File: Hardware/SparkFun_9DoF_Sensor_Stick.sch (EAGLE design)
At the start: 30 parts, among them U1 ITG-3200, U2 ADXL345, U4 3.3V

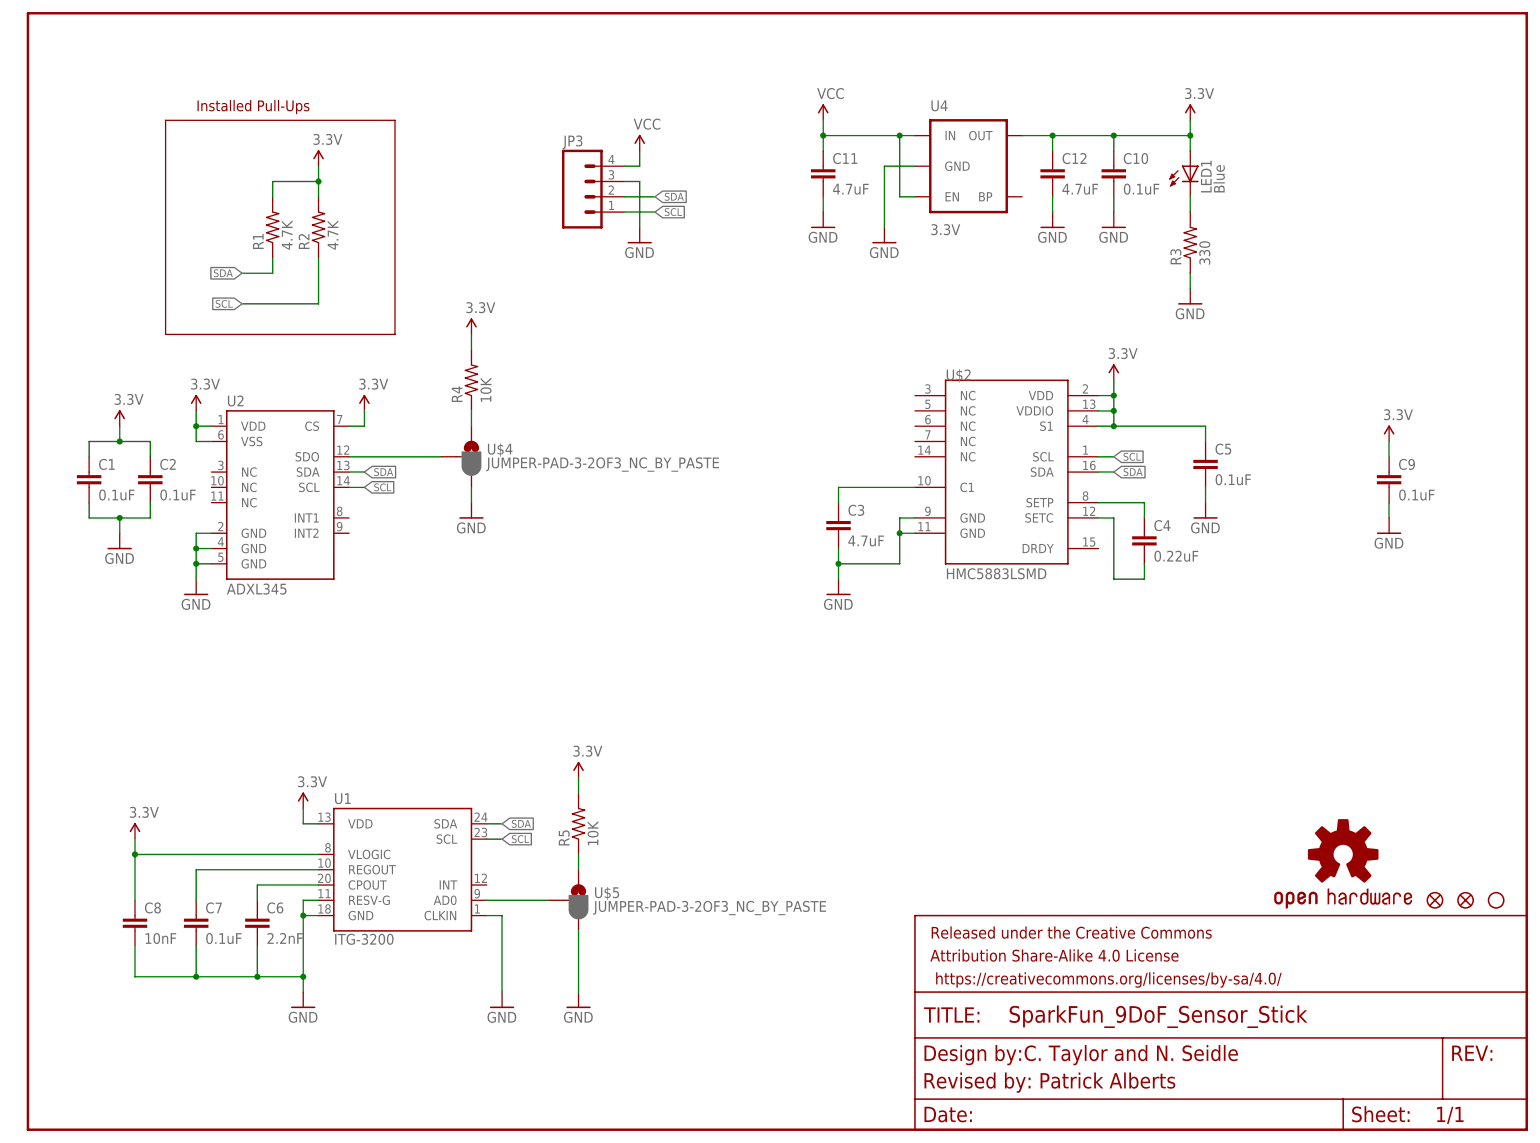
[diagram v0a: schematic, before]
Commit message: Adding in git files, updating to current boards on SF, cleaning up README
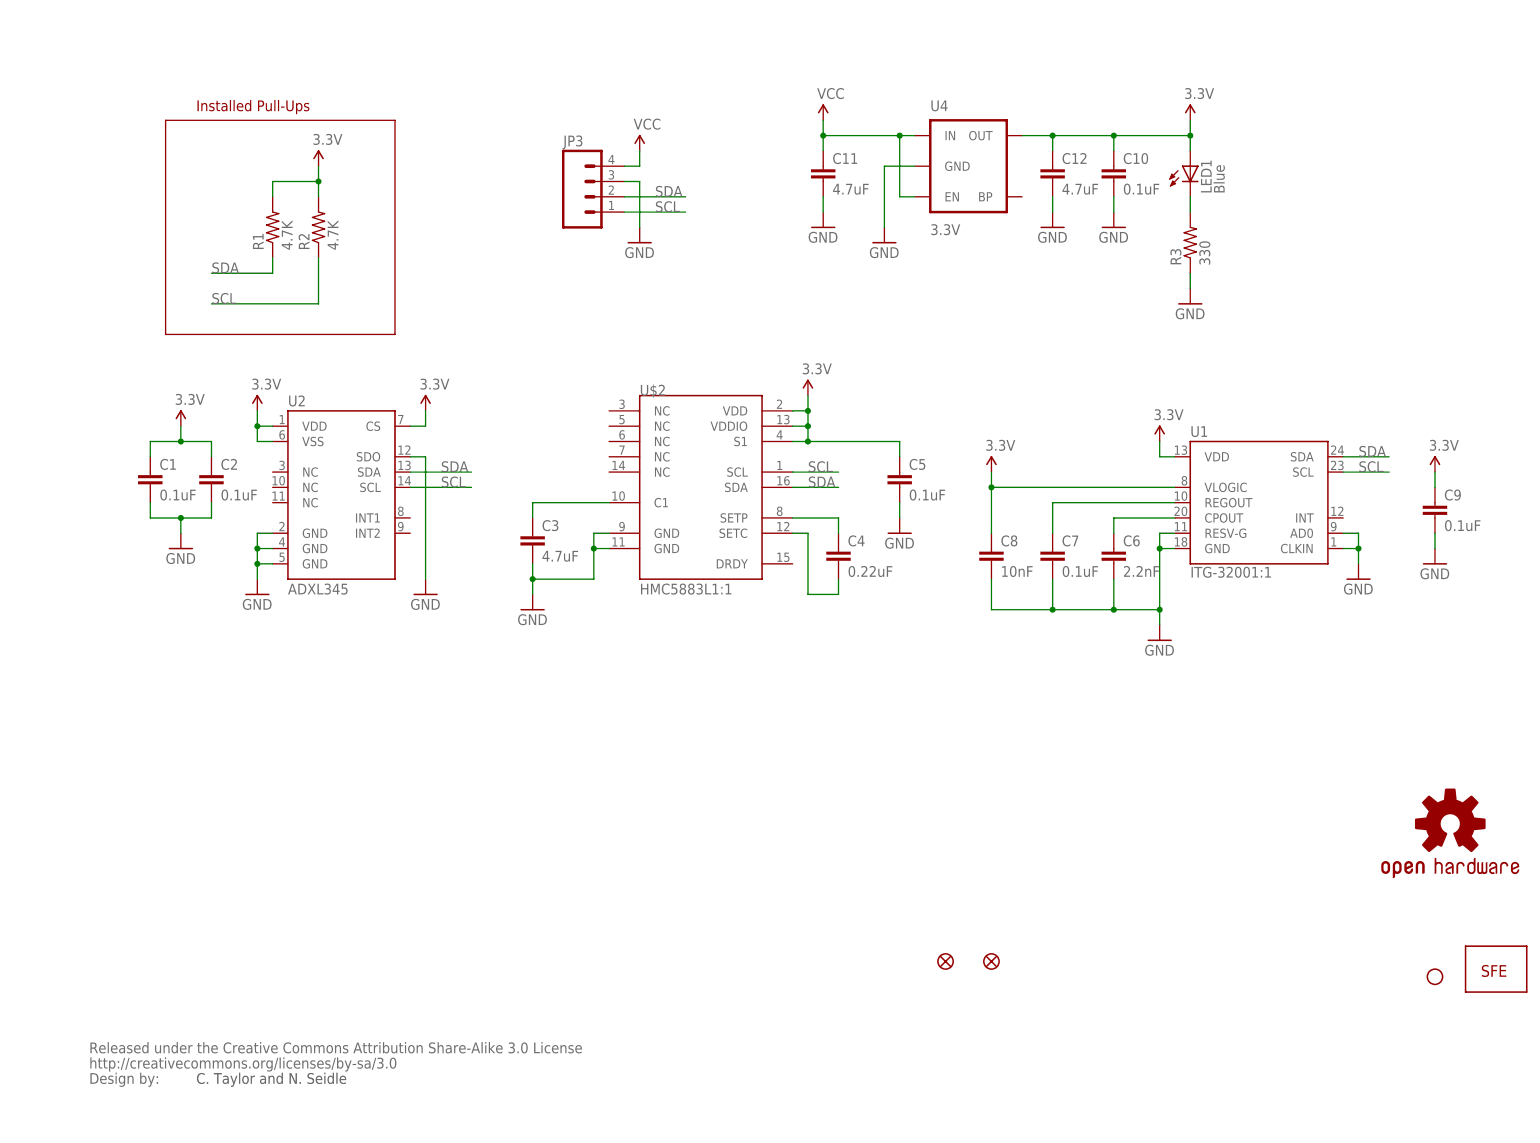
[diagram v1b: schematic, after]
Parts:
- removed FRAME1: FRAME-LETTER, SparkFun-Aesthetics:FRAME-LETTER
- removed R4, R5: 10K, SparkFun-Resistors:10KOHM1/10W1%(0603)0603
- removed U$4, U$5: JUMPER-PAD-3-2OF3_NC_BY_PASTE, SparkFun-Passives:JUMPER-PAD-3-2OF3_NC_BY_PASTE
- added JP4: LOGO-SFESK, SparkFun:LOGO-SFESK
- added U$1: CREATIVE_COMMONS, SparkFun:CREATIVE_COMMONS
- C1, C10, C2, C5, C7, C9: device SparkFun-Capacitors:0.1UF-25V(+80/-20%)(0603) -> SparkFun:CAP0402-CAP
- C11, C12, C3: device SparkFun-Capacitors:4.7UF-6.3V-10%(0603)0603 -> SparkFun:CAP0402-CAP
- C4: device SparkFun-Capacitors:0.22UF-25V-10%(0603) -> SparkFun:CAP0402-CAP
- C6: device SparkFun-Capacitors:2.2NF/2200PF-50V-10%(0603) -> SparkFun:CAP0402-CAP
- C8: device SparkFun-Capacitors:10NF/10000PF-50V-10%(0603) -> SparkFun:CAP0402-CAP
- R1, R2: device SparkFun-Resistors:4.7KOHM1/10W1%(0603) -> SparkFun:RESISTOR0402-RES
- R3: device SparkFun-Resistors:330OHM1/10W1%(0603) -> SparkFun:RESISTOR0402-RES
- U$2: value HMC5883LSMD -> HMC5883L1:1; device SparkFun:HMC5883LSMD -> Testing:HMC5883L1:1
- U1: value ITG-3200 -> ITG-32001:1; device SparkFun:ITG-3200 -> Testing:ITG-32001:1
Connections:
- removed net N$10: U$5.2, U1.AD0
- removed net N$6: U$4.2, U2.SDO
- removed net N$8: R4.1, U$4.1
- removed net N$9: R5.1, U$5.1
- net 3.3V: no longer R4.2, R5.2
- net GND: now also U1.AD0, U2.SDO; no longer U$4.3, U$5.3
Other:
- note removed: "Revised by: Patrick Alberts"
- moved on the sheet: C1, C2, C3, C4, C5, C6, C7, C8, C9, U$2, U1, U2

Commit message: Mid revision work - NOT FUNCTIONAL
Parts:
- removed C12: 4.7uF, SparkFun:CAP0402-CAP
- removed LED1: Blue, SparkFun:LED0603
- removed U$1: CREATIVE_COMMONS, SparkFun:CREATIVE_COMMONS
- removed U$2: HMC5883L1:1, Testing:HMC5883L1:1
- added C13: 10uF, SparkFun-Capacitors:10UF-16V-10%(TANT)
- added D1: RED, SparkFun-LED:LED-RED0603
- added FRAME1: (no value), SparkFun-Aesthetics:FRAME-LETTER
- added SJ1: JUMPER-PAD-3-NC_BY_PASTE, SparkFun-Passives:JUMPER-PAD-3-NC_BY_PASTE
- added SJ2, SJ3, SJ4: JUMPER-PAD-2-NC_BY_TRACE, SparkFun-Passives:JUMPER-PAD-2-NC_BY_TRACE
- added U$4: REVISION, SparkFun-Aesthetics:REVISION
- added U3: 3.3V/150mA, SparkFun-PowerIC:V_REG_MIC52053.3V
- C1, C10, C2, C5, C7, C9: device SparkFun:CAP0402-CAP -> SparkFun-Capacitors:0.1UF-25V(+80/-20%)(0603)
- C11, C3: device SparkFun:CAP0402-CAP -> SparkFun-Capacitors:4.7UF-6.3V-10%(0603)0603
- C4: device SparkFun:CAP0402-CAP -> SparkFun-Capacitors:0.22UF-25V-10%(0603)
- C6: device SparkFun:CAP0402-CAP -> SparkFun-Capacitors:2.2NF/2200PF-50V-10%(0603)
- C8: device SparkFun:CAP0402-CAP -> SparkFun-Capacitors:10NF/10000PF-50V-10%(0603)
- JP1, JP2: device SparkFun:FIDUCIAL1X2 -> SparkFun-Aesthetics:FIDUCIAL1X2
- JP3: device SparkFun:M04PTH -> SparkFun-Connectors:M04PTH
- JP4: value LOGO-SFESK -> SFE_LOGO_FLAME.1_INCH; device SparkFun:LOGO-SFESK -> SparkFun-Aesthetics:SFE_LOGO_FLAME.1_INCH
- JP5: device SparkFun:STAND-OFF -> SparkFun-Electromechanical:STAND-OFF
- R1, R2: device SparkFun:RESISTOR0402-RES -> SparkFun-Resistors:4.7KOHM-1/10W-1%(0603)
- R3: device SparkFun:RESISTOR0402-RES -> SparkFun-Resistors:330OHM1/10W1%(0603)
- U$3: device SparkFun:OSHW-LOGOS -> SparkFun-Aesthetics:OSHW-LOGOS
- U1: device Testing:ITG-32001:1 -> SparkFun-Sensors:ITG-32001:1
- U2: value ADXL345 -> ADXL345"; device SparkFun:ADXL345 -> SparkFun-Sensors:ADXL345"
- U4: value 3.3V -> HMC5883LSMD; device SparkFun:V_REG_LDOSMD -> SparkFun-Sensors:HMC5883LSMD
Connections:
- new net N$10: SJ2.2, U2.SDO
- new net N$12: C5.1, SJ4.2, U4.S1, U4.VDD, U4.VDDIO
- new net N$6: R1.2, SJ1.3
- new net N$8: R2.2, SJ1.1
- new net N$9: SJ3.2, U1.AD0
- net 3.3V: now also C13.+, D1.A, SJ1.2, SJ4.1, U2.VS, U3.OUT; no longer C12.1, C5.1, LED1.A, R1.2, R2.2, U$2.S1, U$2.VDD, U$2.VDDIO, U2.VSS, U4.OUT
- net GND: now also C13.-, JP3.1, SJ2.1, SJ3.1, U3.GND, U4.GND@1, U4.GND@2; no longer C12.2, JP3.3, U$2.GND@1, U$2.GND@2, U1.AD0, U2.SDO, U4.GND
- net N$1: now also U4.C1; no longer U$2.C1
- net N$2: now also U4.SETP; no longer U$2.SETP
- net N$3: now also U4.SETC; no longer U$2.SETC
- net N$4: now also D1.C; no longer LED1.C
- net SCL: now also JP3.4, U4.SCL; no longer JP3.1, U$2.SCL
- net SDA: now also JP3.3, U4.SDA; no longer JP3.2, U$2.SDA
- net VCC: now also JP3.2, U3.EN, U3.IN; no longer JP3.4, U4.EN, U4.IN
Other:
- note added: "Accelerometer"
- note added: "Deafult Address:"
- note added: "Headers"
- note added: "MEMS Gyroscope"
- note added: "Magnetometer"
- note added: "Power System"
- note added: "Toni Klopfenstein"
- note added: "VCC:"
- note added: "v16"
- moved on the sheet: C1, C10, C11, C2, C3, C4, C5, C6, C7, C8, C9, JP3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

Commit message: horizontal orientation
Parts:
- JP1, JP2: value FIDUCIAL1X2 -> FIDUCIALUFIDUCIAL; device SparkFun-Aesthetics:FIDUCIAL1X2 -> SparkFun-Aesthetics:FIDUCIALUFIDUCIAL
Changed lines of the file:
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@@
 <layer number="255" name="routoute" color="7" fill="1" visible="yes" active="yes"/>
 </layers>
-<schematic xreflabel="%F%N/%S" xrefpart="/%S.%C%R">
+<schematic xreflabel="%F%N/%S" xrefpart="/%S">
 <attributes>
 </attributes>
@@
 <part name="P+11" library="SparkFun-Aesthetics" deviceset="3.3V" device=""/>
 <part name="GND15" library="SparkFun-Aesthetics" deviceset="GND" device=""/>
-<part name="JP1" library="SparkFun-Aesthetics" deviceset="FIDUCIAL" device="1X2"/>
+<part name="JP1" library="SparkFun-Aesthetics" deviceset="FIDUCIAL" device="UFIDUCIAL" value="FIDUCIALUFIDUCIAL"/>
 <part name="P+8" library="SparkFun-Aesthetics" deviceset="3.3V" device=""/>
-<part name="JP2" library="SparkFun-Aesthetics" deviceset="FIDUCIAL" device="1X2"/>
+<part name="JP2" library="SparkFun-Aesthetics" deviceset="FIDUCIAL" device="UFIDUCIAL" value="FIDUCIALUFIDUCIAL"/>
 <part name="U4" library="SparkFun-Sensors" deviceset="HMC5883L" device="SMD"/>
 <part name="C3" library="SparkFun-Capacitors" deviceset="4.7UF-6.3V-10%(0603)" device="0603" value="4.7uF"/>

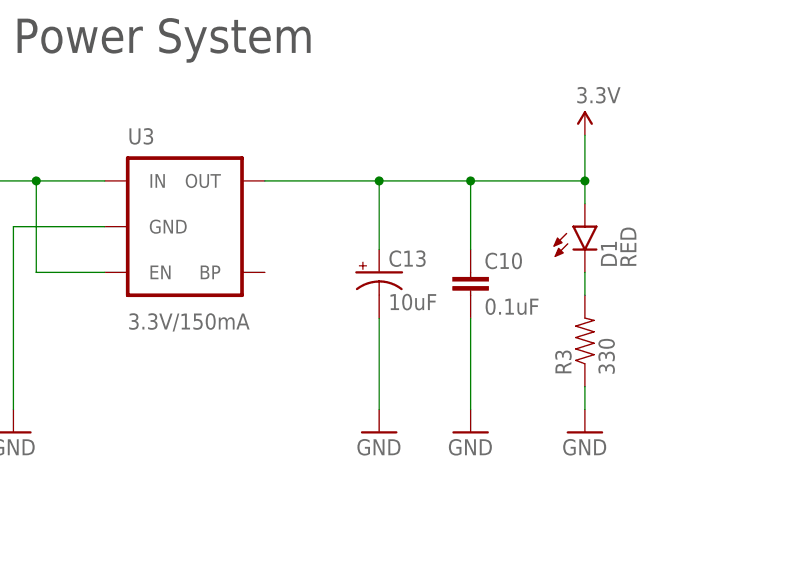
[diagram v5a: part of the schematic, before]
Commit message: No airwires!
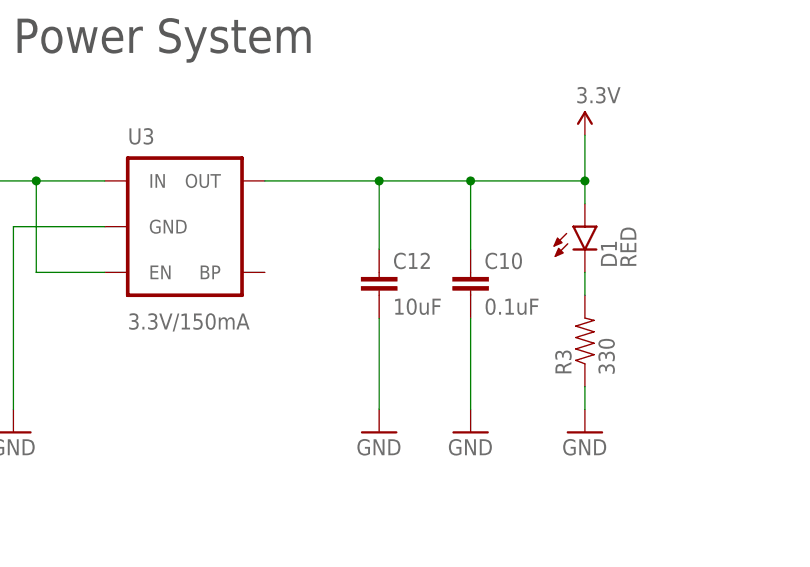
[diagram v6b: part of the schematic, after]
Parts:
- removed C13: 10uF, SparkFun-Capacitors:10UF-16V-10%(TANT)
- added C12: 10uF, SparkFun-Capacitors:10UF-6.3V-20%(0603)
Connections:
- net 3.3V: now also C12.1; no longer C13.+
- net GND: now also C12.2; no longer C13.-
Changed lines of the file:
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@@
 <part name="U3" library="SparkFun-PowerIC" deviceset="V_REG_MIC5205" device="3.3V" value="3.3V/150mA"/>
 <part name="SJ1" library="SparkFun-Passives" deviceset="JUMPER-PAD-3-NC_BY_PASTE" device=""/>
-<part name="C13" library="SparkFun-Capacitors" deviceset="10UF-16V-10%(TANT)" device="" value="10uF"/>
 <part name="SJ2" library="SparkFun-Passives" deviceset="JUMPER-PAD-2-NC_BY_TRACE" device=""/>
 <part name="SJ3" library="SparkFun-Passives" deviceset="JUMPER-PAD-2-NC_BY_TRACE" device=""/>
@@
 <part name="SJ4" library="SparkFun-Passives" deviceset="JUMPER-PAD-2-NC_BY_TRACE" device=""/>
 <part name="P+12" library="SparkFun-Aesthetics" deviceset="3.3V" device=""/>
+<part name="C12" library="SparkFun-Capacitors" deviceset="10UF-6.3V-20%(0603)" device="" value="10uF"/>
 </parts>
 <sheets>
@@
 <attribute name="NAME" x="48.26" y="74.041" size="1.778" layer="95"/>
 </instance>
-<instance part="C13" gate="G$1" x="190.5" y="76.2"/>
 <instance part="SJ2" gate="G$1" x="60.96" y="137.16" smashed="yes" rot="MR90">
 <attribute name="NAME" x="63.5" y="134.62" size="1.778" layer="95" rot="MR90"/>
@@
 </instance>
 <instance part="P+12" gate="G$1" x="147.32" y="170.18"/>
+<instance part="C12" gate="G$1" x="190.5" y="73.66"/>
 </instances>
 <busses>
@@
 <pinref part="P+11" gate="G$1" pin="3.3V"/>
 <pinref part="U3" gate="U1" pin="OUT"/>
-<pinref part="C13" gate="G$1" pin="+"/>
+<pinref part="C12" gate="G$1" pin="1"/>
 </segment>
 <segment>
@@
 <wire x1="190.5" y1="60.96" x2="190.5" y2="71.12" width="0.1524" layer="91"/>
 <pinref part="GND9" gate="1" pin="GND"/>
-<pinref part="C13" gate="G$1" pin="-"/>
-</segment>
-<segment>
+<pinref part="C12" gate="G$1" pin="2"/>
+</segment>
+<segment>

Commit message: Updating for QC checks
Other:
- note added: "Jumper can be opened to change I2C address Default Address: 0x53"
- note added: "Jumper can be opened to change I2C address Default Address: 0x68"
- note added: "Jumper can be opened to cut power to magnetometer. Allows use of multiple 9DOF Sticks on the same I2C bus."
- note added: "Logic is 3.3V"
- note added: "VCC: 3.3V-5V"
- note removed: "Deafult Address:"
- note removed: "VCC:"
- moved on the sheet: C3, C4, C5, C6, C7, C8, C9, SJ3, SJ4, U1, U4

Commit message: Changes from engineering review
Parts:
- removed SJ2: JUMPER-PAD-2-NC_BY_TRACE, SparkFun-Passives:JUMPER-PAD-2-NC_BY_TRACE
- added R4, R5: DNP, SparkFun-Resistors:RESISTOR0603
- added SJ5: JUMPER-PAD-3-2OF3_NC_BY_TRACE_LARGE, SparkFun-Passives:JUMPER-PAD-3-2OF3_NC_BY_TRACE_LARGE
- SJ3: value JUMPER-PAD-2-NC_BY_TRACE -> JUMPER-PAD-3-2OF3_NC_BY_TRACE_LARGE; device SparkFun-Passives:JUMPER-PAD-2-NC_BY_TRACE -> SparkFun-Passives:JUMPER-PAD-3-2OF3_NC_BY_TRACE_LARGE
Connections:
- new net N$11: R4.1, SJ3.1
- new net N$13: R5.1, SJ5.1
- net 3.3V: now also R4.2, R5.2
- net GND: now also SJ3.3, SJ5.3; no longer SJ2.1, SJ3.1
- net N$10: now also SJ5.2; no longer SJ2.2
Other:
- note added: "Jumper can be opened to change I2C address Default Address: 0x53 Alternate Addr: 0x1D User must also add R5"
- note added: "Jumper can be opened to change I2C address Default Address: 0x68 Alternate Addr: 0x69 User must also add R4"
- note added: "Jumper can be opened to cut power to magnetometer. Allows use of multiple 9DOF Sticks on the same I2C bus. Default Addr: 0x1E"
- note removed: "Jumper can be opened to change I2C address Default Address: 0x53"
- note removed: "Jumper can be opened to change I2C address Default Address: 0x68"
- note removed: "Jumper can be opened to cut power to magnetometer. Allows use of multiple 9DOF Sticks on the same I2C bus."
- moved on the sheet: C10, C11, C12, C6, C7, C9, D1, JP3, R1, R2, R3, SJ1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
